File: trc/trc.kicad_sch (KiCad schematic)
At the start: 25 parts, among them J1 PWR, J2 Control, J3 Inverter, J4 BMS, J5 States, J6 Relays

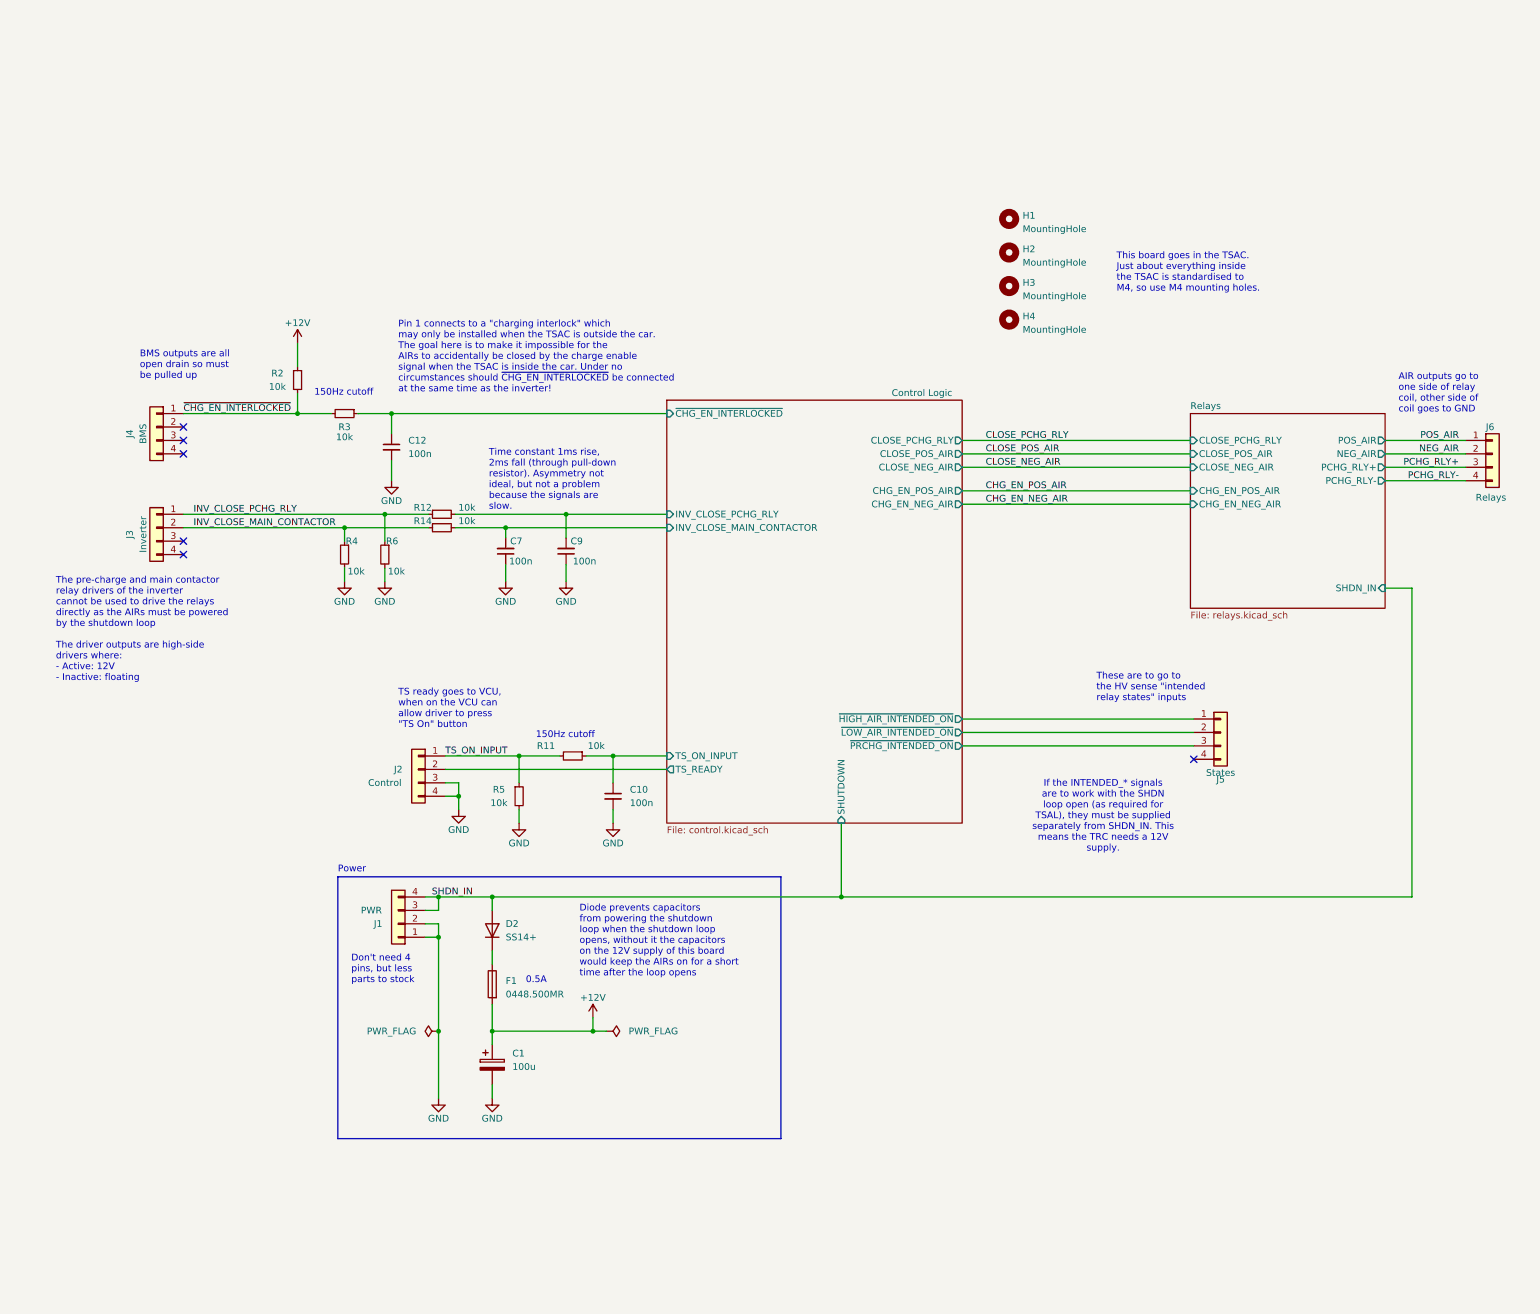
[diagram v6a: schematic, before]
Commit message: Added green light to TRC
Began Layout
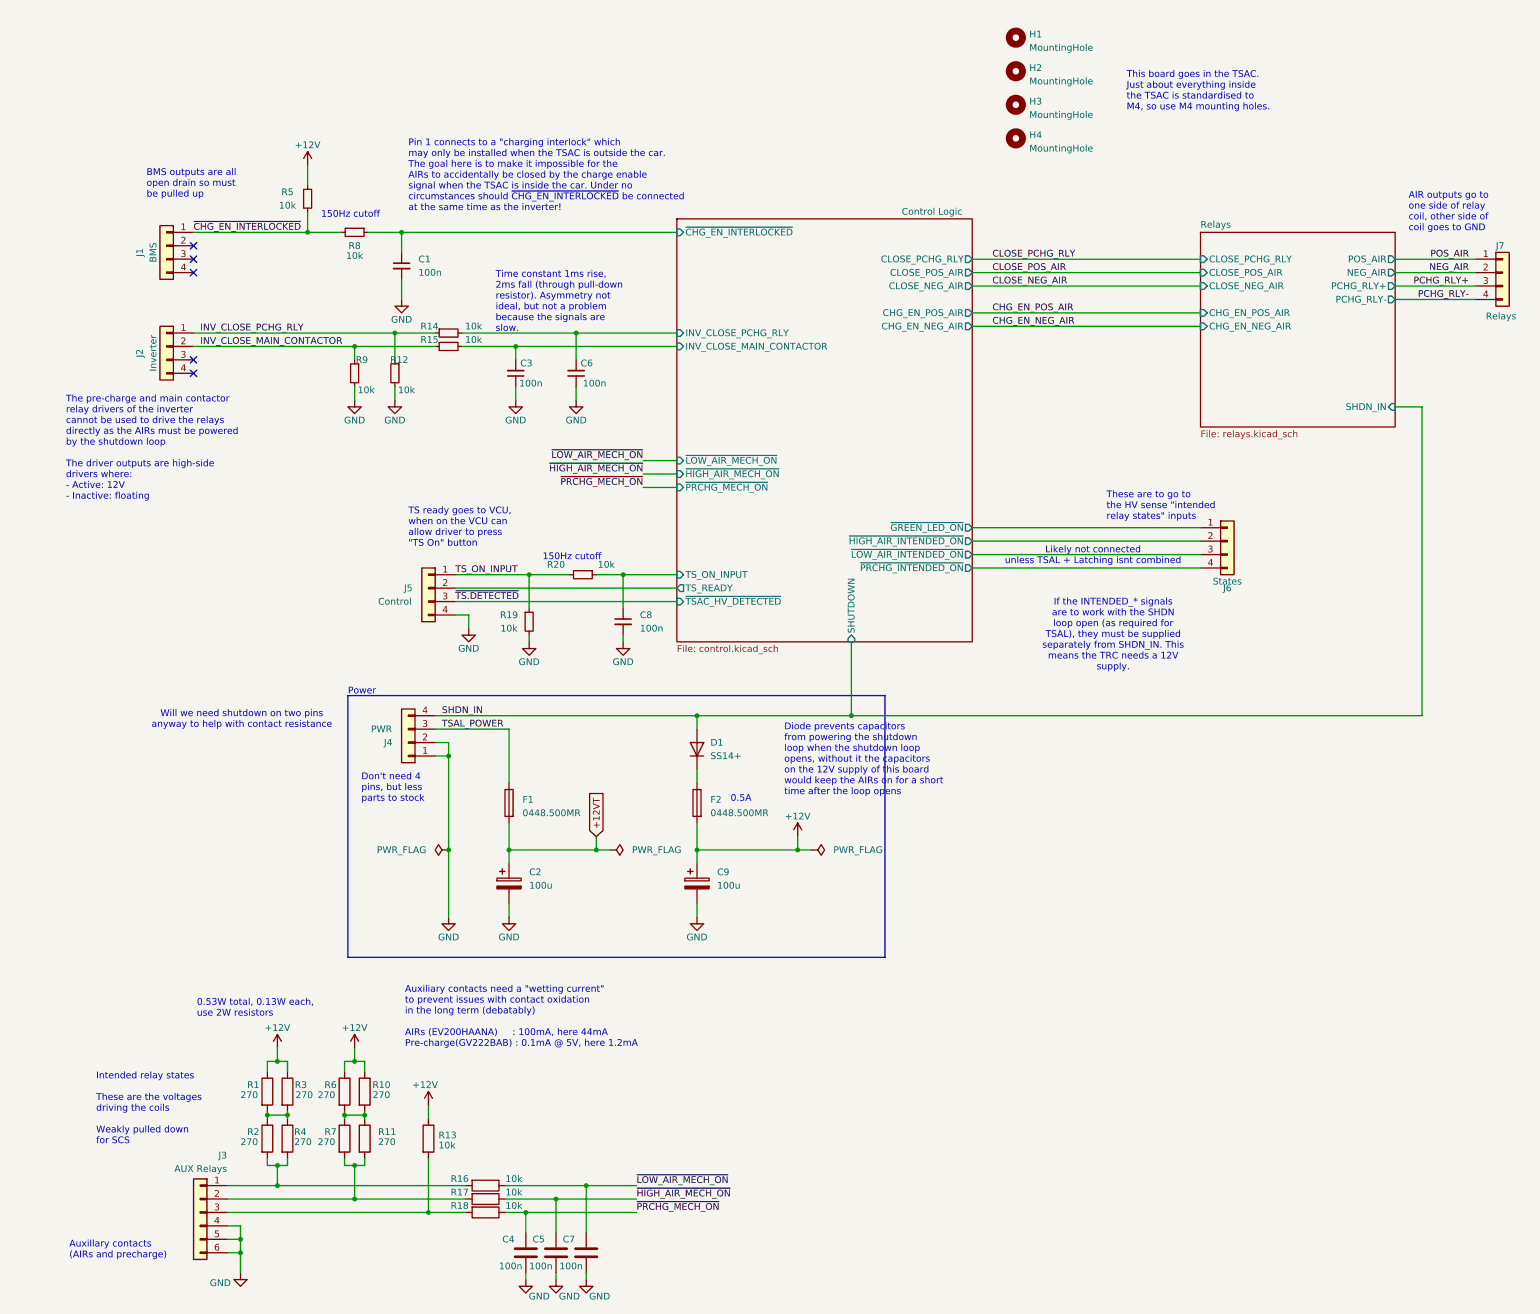
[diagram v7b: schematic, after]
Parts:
- removed J5: States, Connector_Molex:Molex_Micro-Fit_3.0_43045-0412_2x02_P3.00mm_Vertical, symbol Connector_Generic:Conn_01x04
- added C2: 100u, Capacitor_THT:CP_Radial_D5.0mm_P2.00mm, symbol Device:C_Polarized
- added C4, C5, C7: 100n, Capacitor_SMD:C_0805_2012Metric_Pad1.18x1.45mm_HandSolder, symbol Device:C
- added F1: 0448.500MR, Fuse:Fuse_Littelfuse-NANO2-451_453, symbol Device:Fuse
- added J3: AUX Relays, SUFST:Molex_Micro-Fit_3.0_43045-0612_2x03_P3.00mm_Vertical, symbol Connector_Generic:Conn_01x06
- added J6: States, Connector_Molex:Molex_Micro-Fit_3.0_43045-0412_2x02_P3.00mm_Vertical, symbol Connector_Generic:Conn_01x04
- added R1, R10, R11, R2, R3, R4, R6, R7: 270, Resistor_SMD:R_2512_6332Metric, symbol Device:R
- added R13, R16, R17, R18: 10k, Resistor_SMD:R_0805_2012Metric_Pad1.20x1.40mm_HandSolder, symbol Device:R
- renumbered C12 to C1, C7 to C3, C9 to C6, C10 to C8, C1 to C9, D2 to D1, F1 to F2, J4 to J1, J3 to J2, J1 to J4, J2 to J5, J6 to J7, R6 to R12, R12 to R14, R14 to R15, R5 to R19, R11 to R20, R2 to R5, R3 to R8, R4 to R9
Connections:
- net +12V: now also R1.1, R10.1, R13.1, R3.1, R6.1
- net Control Logic/~{HIGH_AIR_INTENDED_ON}: now also J6.2 (Pin_2)
- net Control Logic/~{LOW_AIR_INTENDED_ON}: now also J6.3 (Pin_3)
- net Control Logic/~{PRCHG_INTENDED_ON}: now also J6.4 (Pin_4)
- net GND: now also C2.2, C4.2, C5.2, C7.2, J3.4 (Pin_4), J3.5 (Pin_5), J3.6 (Pin_6); no longer J5.3 (Pin_3)
- net SHDN_IN: no longer J4.3 (Pin_3)
- new net: J3.3 (Pin_3), R13.2, R18.2
- new net: R1.2, R2.1, R3.2, R4.1
- new net: R10.2, R11.1, R6.2, R7.1
- new net: J3.2 (Pin_2), R11.2, R17.2, R7.2
- new net: J3.1 (Pin_1), R16.2, R2.2, R4.2
- new net +12VT: C2.1, F1.2
- new net Control Logic/~{GREEN_LED_ON}: J6.1 (Pin_1)
- new net TSAL_POWER: F1.1, J4.3 (Pin_3)
- new net ~{HIGH_AIR_MECH_ON}: C5.1, R17.1
- new net ~{LOW_AIR_MECH_ON}: C7.1, R16.1
- new net ~{PRCHG_MECH_ON}: C4.1, R18.1
- new net ~{TS.DETECTED}: J5.3 (Pin_3)
- no-connect marks 6 -> 5
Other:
- sheet Control Logic ports: added ~{GREEN_LED_ON}, ~{HIGH_AIR_MECH_ON}, ~{LOW_AIR_MECH_ON}, ~{PRCHG_MECH_ON}, ~{TSAC_HV_DETECTED}; removed none
- note added: "0.53W total, 0.13W each, use 2W resistors"
- note added: "Auxiliary contacts need a "wetting current" to prevent issues with contact oxidation in the long term (debatably) AIRs (EV200HAANA) : 100mA, here 44mA Pre-charge(GV222BAB) : 0.1mA @ 5V, here 1.2mA"
- note added: "Auxillary contacts (AIRs and precharge)"
- note added: "Intended relay states These are the voltages driving the coils Weakly pulled down for SCS"
- note added: "Likely not connected unless TSAL + Latching isnt combined"
- note added: "Will we need shutdown on two pins anyway to help with contact resistance"
- moved on the sheet: C1, C3, C6, C8, C9, D1, F2, H1, H2, H3, H4, J1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

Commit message: Initial Layout of PCB complete
TODO: Add SS relay into design
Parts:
- removed J1: BMS, Connector_Molex:Molex_Micro-Fit_3.0_43045-0412_2x02_P3.00mm_Vertical, symbol Connector_Generic:Conn_01x04
- removed J2: Inverter, Connector_Molex:Molex_Micro-Fit_3.0_43045-0412_2x02_P3.00mm_Vertical, symbol Connector_Generic:Conn_01x04
- removed J3: AUX Relays, SUFST:Molex_Micro-Fit_3.0_43045-0612_2x03_P3.00mm_Vertical, symbol Connector_Generic:Conn_01x06
- removed J4: PWR, Connector_Molex:Molex_Micro-Fit_3.0_43045-0412_2x02_P3.00mm_Vertical, symbol Connector_Generic:Conn_01x04
- removed J5: Control, Connector_Molex:Molex_Micro-Fit_3.0_43045-0412_2x02_P3.00mm_Vertical, symbol Connector_Generic:Conn_01x04
- removed J6: States, Connector_Molex:Molex_Micro-Fit_3.0_43045-0412_2x02_P3.00mm_Vertical, symbol Connector_Generic:Conn_01x04
- removed J7: Relays, Connector_Molex:Molex_Micro-Fit_3.0_43045-0412_2x02_P3.00mm_Vertical, symbol Connector_Generic:Conn_01x04
- added J8, J9: Conn_01x12_Socket, Connector_Molex:Molex_Micro-Fit_3.0_43045-1200_2x06_P3.00mm_Horizontal, symbol Connector:Conn_01x12_Socket
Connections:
- net GND: now also J8.4 (Pin_4), J8.5 (Pin_5), J8.6 (Pin_6), J9.1 (Pin_1), J9.9 (Pin_9)
- net INV_CLOSE_MAIN_CONTACTOR: now also J9.8 (Pin_8)
- net INV_CLOSE_PCHG_RLY: now also J9.2 (Pin_2)
- net NEG_AIR: now also J9.11 (Pin_11)
- net PCHG_RLY+: now also J9.5 (Pin_5)
- net PCHG_RLY-: now also J9.4 (Pin_4)
- net POS_AIR: now also J9.12 (Pin_12)
- net SHDN_IN: now also J9.10 (Pin_10)
- net TSAL_POWER: now also J9.7 (Pin_7)
- net TS_ON_INPUT: now also J8.7 (Pin_7)
- net ~{CHG_EN_INTERLOCKED}: now also J9.3 (Pin_3)
- net ~{TS.DETECTED}: now also J8.1 (Pin_1)
- net ~{PRCHG_MECH_ON_IN}: now reaches R13.2, R18.2
- net ~{PRCHG_MECH_ON_IN}: now also J8.11 (Pin_11)
- net ~{HIGH_AIR_MECH_ON_IN}: now reaches R11.2, R17.2, R7.2
- net ~{HIGH_AIR_MECH_ON_IN}: now also J8.10 (Pin_10)
- net ~{LOW_AIR_MECH_ON_IN}: now reaches R16.2, R2.2, R4.2
- net ~{LOW_AIR_MECH_ON_IN}: now also J8.9 (Pin_9)
- new net TS_READY: J8.2 (Pin_2)
- new net ~{GREEN_LED_ON}: J8.8 (Pin_8)
- no-connect marks 5 -> 6
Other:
- note added: "Go to tsal and ground box"
- note removed: "Don't need 4 pins, but less parts to stock"
